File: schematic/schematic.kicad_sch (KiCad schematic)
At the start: 25 parts, among them SW1 SW_SPST, U1 ESP32-S3-DevKitC

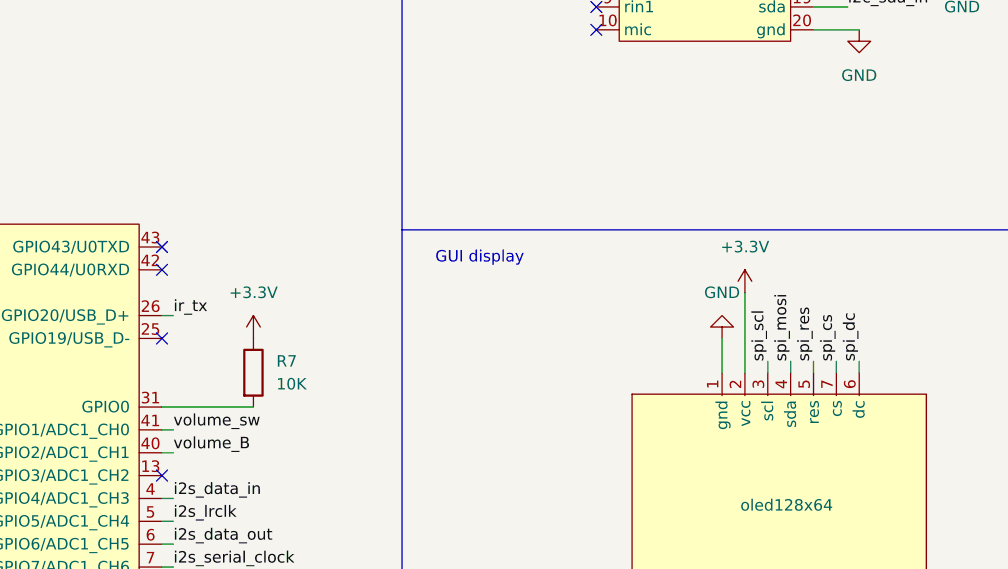
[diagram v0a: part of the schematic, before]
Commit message: Update schematic with note about pullup on GPIO0 for booting from external 5V, bypassing usb.
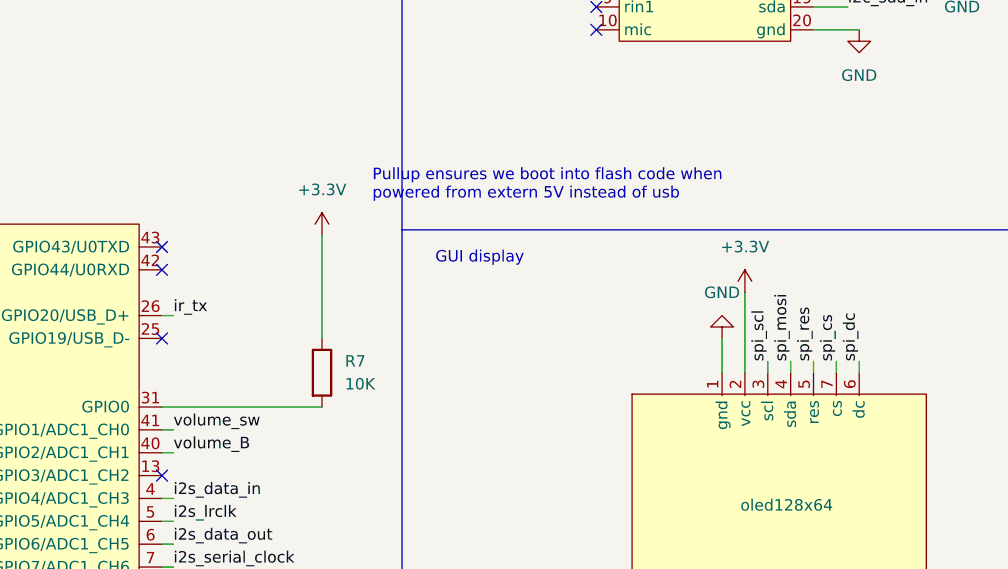
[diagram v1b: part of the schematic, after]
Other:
- note added: "Pullup ensures we boot into flash code when powered from extern 5V instead of usb"
- moved on the sheet: R7
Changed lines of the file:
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@@
 		)
 	)
+	(text "Pullup ensures we boot into flash code when\npowered from extern 5V instead of usb "
+		(exclude_from_sim no)
+		(at 180.848 74.422 0)
+		(effects
+			(font
+				(size 1.27 1.27)
+			)
+			(justify left)
+		)
+	)
 	(text "BOSE IR remote input\nNote: this might not be necessary with\nboot sequence sending AUX and double\nclick on volume sending on/of"
 		(exclude_from_sim no)
@@
 	(wire
 		(pts
+			(xy 175.26 91.44) (xy 175.26 80.01)
+		)
+		(stroke
+			(width 0)
+			(type default)
+		)
+	)
+	(wire
+		(pts
 			(xy 104.14 24.13) (xy 104.14 26.67)
 		)
@@
 	(wire
 		(pts
-			(xy 157.48 99.06) (xy 167.64 99.06)
+			(xy 157.48 99.06) (xy 175.26 99.06)
 		)
 		(stroke
@@
 		)
 		(instances
-			(project ""
+			(project "schematic"
 				(path "/ad99cfc7-1930-4a76-846f-3ad4dbd23fae"
 					(reference "ES8388module")
@@
 		)
 		(instances
-			(project ""
+			(project "schematic"
 				(path "/ad99cfc7-1930-4a76-846f-3ad4dbd23fae"
 					(reference "#PWR04")
@@
 		)
 		(instances
-			(project ""
+			(project "schematic"
 				(path "/ad99cfc7-1930-4a76-846f-3ad4dbd23fae"
 					(reference "#PWR01")
@@
 		)
 		(instances
-			(project ""
+			(project "schematic"
 				(path "/ad99cfc7-1930-4a76-846f-3ad4dbd23fae"
 					(reference "R5")
@@
 		)
 		(instances
-			(project ""
+			(project "schematic"
 				(path "/ad99cfc7-1930-4a76-846f-3ad4dbd23fae"
 					(reference "SW1")
@@
 		)
 		(instances
-			(project ""
+			(project "schematic"
 				(path "/ad99cfc7-1930-4a76-846f-3ad4dbd23fae"
 					(reference "#PWR06")
@@
 		)
 		(instances
-			(project ""
+			(project "schematic"
 				(path "/ad99cfc7-1930-4a76-846f-3ad4dbd23fae"
 					(reference "#PWR027")
@@
 		)
 		(instances
-			(project ""
+			(project "schematic"
 				(path "/ad99cfc7-1930-4a76-846f-3ad4dbd23fae"
 					(reference "#PWR017")
@@
 		)
 		(instances
-			(project ""
+			(project "schematic"
 				(path "/ad99cfc7-1930-4a76-846f-3ad4dbd23fae"
 					(reference "#PWR07")
@@
 		)
 		(instances
-			(project ""
+			(project "schematic"
 				(path "/ad99cfc7-1930-4a76-846f-3ad4dbd23fae"
 					(reference "R10")
@@
 		)
 		(instances
-			(project ""
+			(project "schematic"
 				(path "/ad99cfc7-1930-4a76-846f-3ad4dbd23fae"
 					(reference "C1")
@@
 		)
 		(instances
-			(project ""
+			(project "schematic"
 				(path "/ad99cfc7-1930-4a76-846f-3ad4dbd23fae"
 					(reference "#PWR026")
@@
 		)
 		(instances
-			(project ""
+			(project "schematic"
 				(path "/ad99cfc7-1930-4a76-846f-3ad4dbd23fae"
 					(reference "#PWR05")
@@
 		)
 		(instances
-			(project ""
+			(project "schematic"
 				(path "/ad99cfc7-1930-4a76-846f-3ad4dbd23fae"
 					(reference "#PWR014")
@@
 		)
 		(instances
-			(project ""
+			(project "schematic"
 				(path "/ad99cfc7-1930-4a76-846f-3ad4dbd23fae"
 					(reference "#PWR015")
@@
 		)
 		(instances
-			(project ""
+			(project "schematic"
 				(path "/ad99cfc7-1930-4a76-846f-3ad4dbd23fae"
 					(reference "#PWR03")
@@
 		)
 		(instances
-			(project ""
+			(project "schematic"
 				(path "/ad99cfc7-1930-4a76-846f-3ad4dbd23fae"
 					(reference "#PWR016")
@@
 		)
 		(instances
-			(project ""
+			(project "schematic"
 				(path "/ad99cfc7-1930-4a76-846f-3ad4dbd23fae"
 					(reference "D1")
@@
 		)
 		(instances
-			(project ""
+			(project "schematic"
 				(path "/ad99cfc7-1930-4a76-846f-3ad4dbd23fae"
 					(reference "#PWR09")
@@
 		)
 		(instances
-			(project ""
+			(project "schematic"
 				(path "/ad99cfc7-1930-4a76-846f-3ad4dbd23fae"
 					(reference "#PWR02")
@@
 		)
 		(instances
-			(project ""
+			(project "schematic"
 				(path "/ad99cfc7-1930-4a76-846f-3ad4dbd23fae"
 					(reference "U1")
@@
 		)
 		(instances
-			(project ""
+			(project "schematic"
 				(path "/ad99cfc7-1930-4a76-846f-3ad4dbd23fae"
 					(reference "#PWR013")
@@
 		)
 		(instances
-			(project ""
+			(project "schematic"
 				(path "/ad99cfc7-1930-4a76-846f-3ad4dbd23fae"
 					(reference "oled128x64")
@@
 		)
 		(instances
-			(project ""
+			(project "schematic"
 				(path "/ad99cfc7-1930-4a76-846f-3ad4dbd23fae"
 					(reference "#PWR010")
@@
 		)
 		(instances
-			(project ""
+			(project "schematic"
 				(path "/ad99cfc7-1930-4a76-846f-3ad4dbd23fae"
 					(reference "#PWR028")
@@
 	(symbol
 		(lib_id "Device:R")
-		(at 167.64 95.25 0)
+		(at 175.26 95.25 0)
 		(unit 1)
 		(exclude_from_sim no)
@@
 		(fields_autoplaced yes)
 		(property "Reference" "R7"
-			(at 170.18 93.9799 0)
+			(at 177.8 93.9799 0)
 			(effects
 				(font
@@
 		)
 		(property "Value" "10K"
-			(at 170.18 96.5199 0)
+			(at 177.8 96.5199 0)
 			(effects
 				(font
@@
 		)
 		(property "Footprint" ""
-			(at 165.862 95.25 90)
+			(at 173.482 95.25 90)
 			(effects
 				(font
@@
 		)
 		(property "Datasheet" "~"
-			(at 167.64 95.25 0)
+			(at 175.26 95.25 0)
 			(effects
 				(font
@@
 		)
 		(property "Description" "Resistor"
-			(at 167.64 95.25 0)
+			(at 175.26 95.25 0)
 			(effects
 				(font
@@
 		)
 		(instances
-			(project ""
+			(project "schematic"
 				(path "/ad99cfc7-1930-4a76-846f-3ad4dbd23fae"
 					(reference "R7")
@@
 		)
 		(instances
-			(project ""
+			(project "schematic"
 				(path "/ad99cfc7-1930-4a76-846f-3ad4dbd23fae"
 					(reference "#PWR019")
@@
 	(symbol
 		(lib_id "power:+3.3V")
-		(at 167.64 91.44 0)
+		(at 175.26 80.01 0)
 		(unit 1)
 		(exclude_from_sim no)
@@
 		(fields_autoplaced yes)
 		(property "Reference" "#PWR029"
-			(at 167.64 95.25 0)
+			(at 175.26 83.82 0)
 			(effects
 				(font
@@
 		)
 		(property "Value" "+3.3V"
-			(at 167.64 86.36 0)
+			(at 175.26 74.93 0)
 			(effects
 				(font
@@
 		)
 		(property "Footprint" ""
-			(at 167.64 91.44 0)
+			(at 175.26 80.01 0)
 			(effects
 				(font
@@
 		)
 		(property "Datasheet" ""
-			(at 167.64 91.44 0)
+			(at 175.26 80.01 0)
 			(effects
 				(font
@@
 		)
 		(property "Description" "Power symbol creates a global label with name \"+3.3V\""
-			(at 167.64 91.44 0)
+			(at 175.26 80.01 0)
 			(effects
 				(font
@@
 		)
 		(instances
-			(project ""
+			(project "schematic"
 				(path "/ad99cfc7-1930-4a76-846f-3ad4dbd23fae"
 					(reference "#PWR029")
@@
 		)
 		(instances
-			(project ""
+			(project "schematic"
 				(path "/ad99cfc7-1930-4a76-846f-3ad4dbd23fae"
 					(reference "R2")
@@
 		)
 		(instances
-			(project ""
+			(project "schematic"
 				(path "/ad99cfc7-1930-4a76-846f-3ad4dbd23fae"
 					(reference "volume")
@@
 		)
 		(instances
-			(project ""
+			(project "schematic"
 				(path "/ad99cfc7-1930-4a76-846f-3ad4dbd23fae"
 					(reference "C3")
@@
 		)
 		(instances
-			(project ""
+			(project "schematic"
 				(path "/ad99cfc7-1930-4a76-846f-3ad4dbd23fae"
 					(reference "R1")
@@
 		)
 		(instances
-			(project ""
+			(project "schematic"
 				(path "/ad99cfc7-1930-4a76-846f-3ad4dbd23fae"
 					(reference "bose_on_sw")
@@
 		)
 		(instances
-			(project ""
+			(project "schematic"
 				(path "/ad99cfc7-1930-4a76-846f-3ad4dbd23fae"
 					(reference "#PWR08")

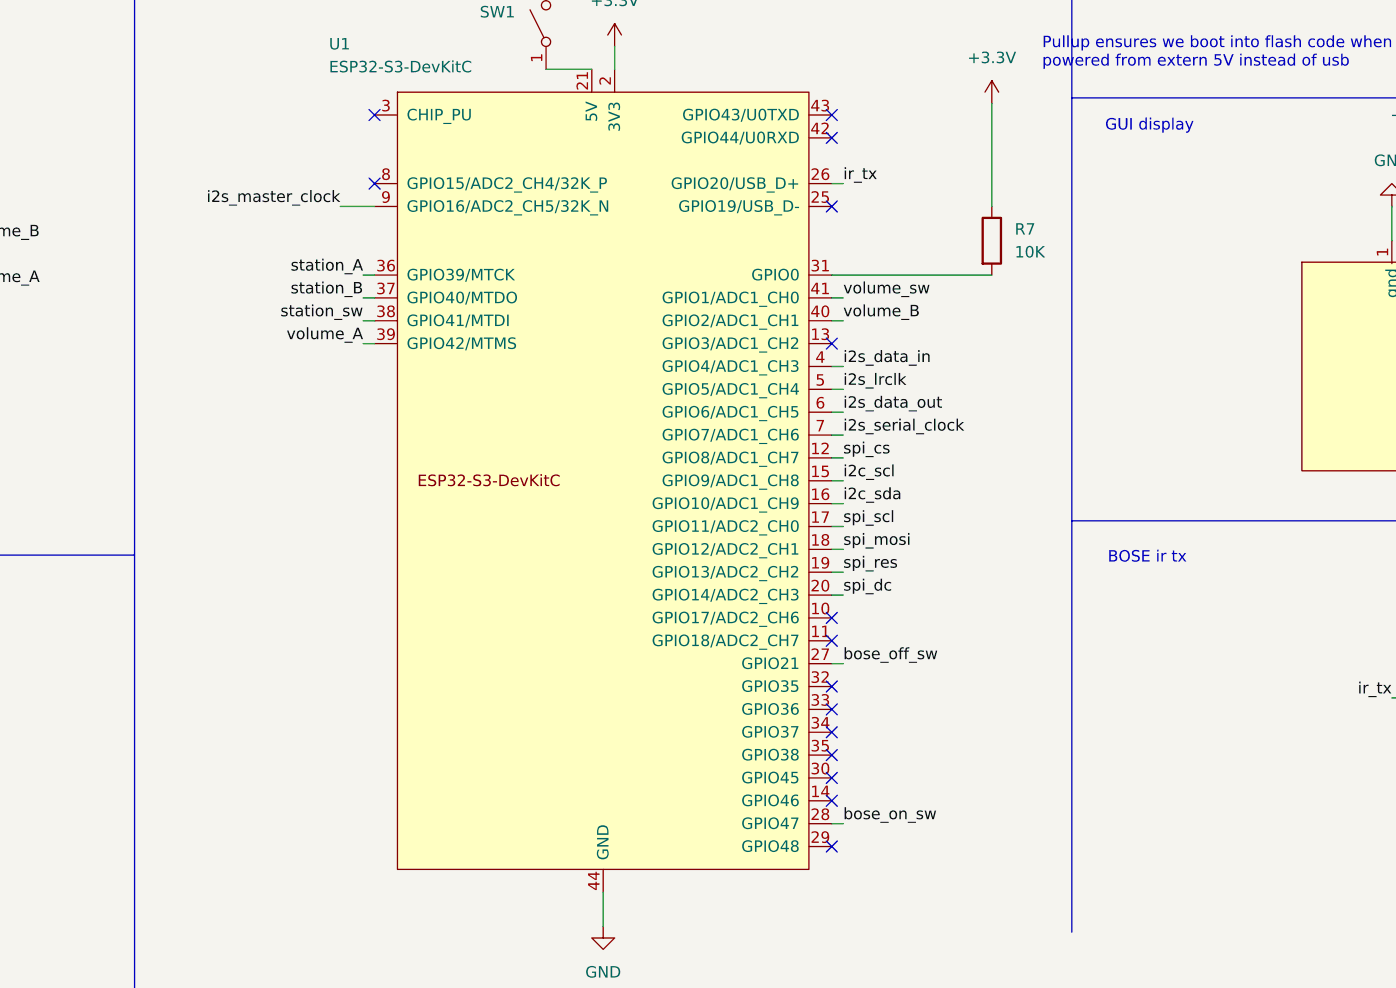
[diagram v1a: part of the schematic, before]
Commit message: update gpio assignments on schematic.
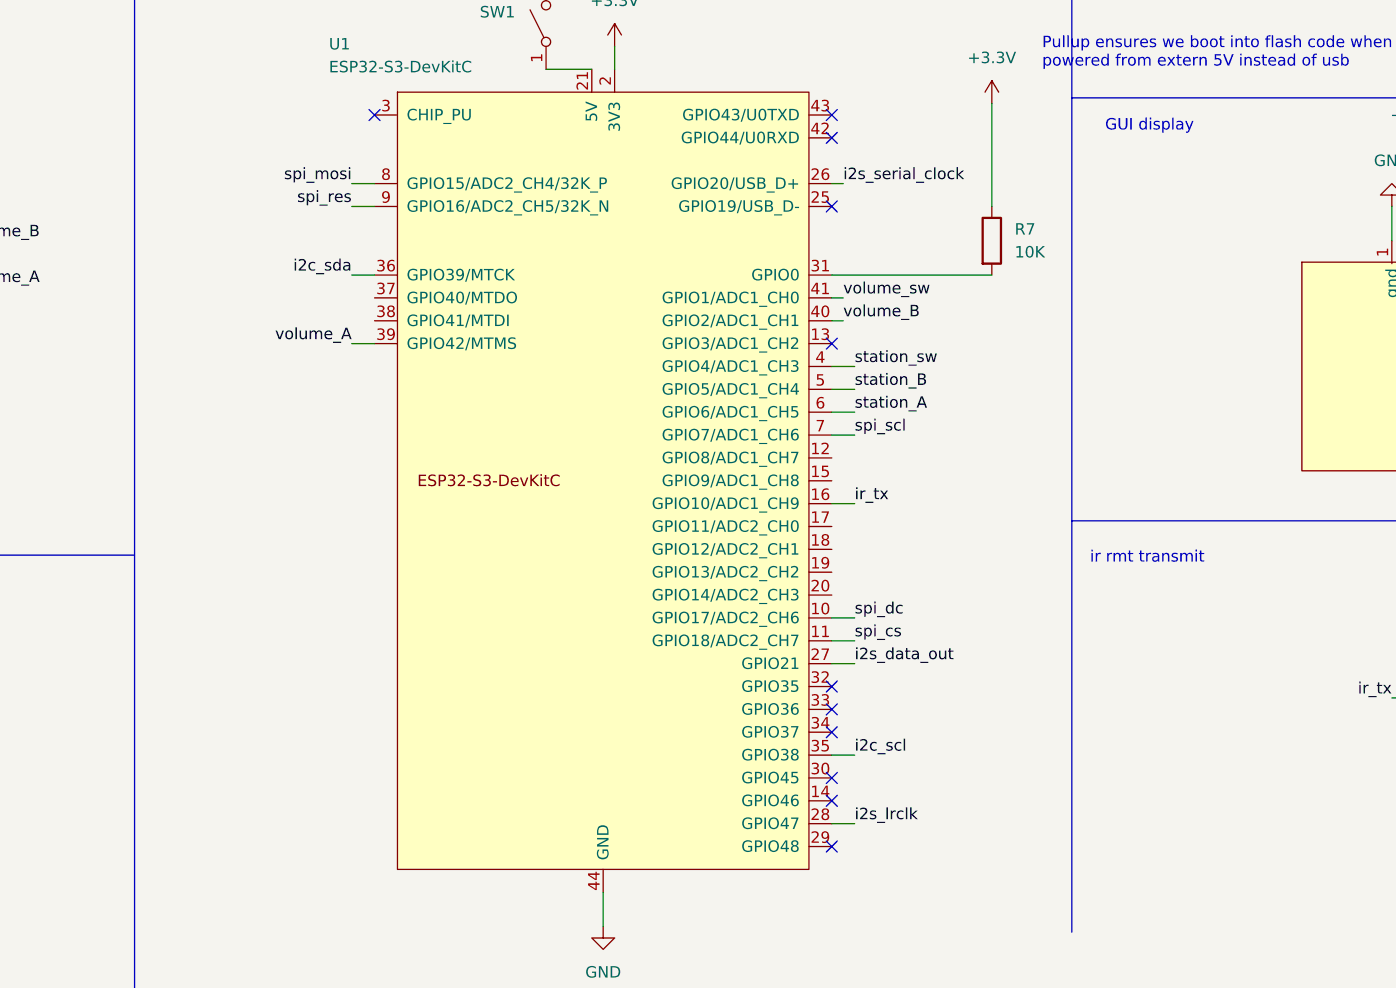
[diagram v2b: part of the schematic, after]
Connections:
- net bose_off_sw: no longer U1.27 (GPIO21)
- net bose_on_sw: no longer U1.28 (GPIO47)
- net i2c_scl: now also U1.35 (GPIO38); no longer U1.15 (GPIO9/ADC1_CH8)
- net i2c_sda: now also U1.36 (GPIO39/MTCK); no longer U1.16 (GPIO10/ADC1_CH9)
- net i2s_data_in: no longer U1.4 (GPIO4/ADC1_CH3)
- net i2s_data_out: now also U1.27 (GPIO21); no longer U1.6 (GPIO6/ADC1_CH5)
- net i2s_lrclk: now also U1.28 (GPIO47); no longer U1.5 (GPIO5/ADC1_CH4)
- net i2s_master_clock: no longer U1.9 (GPIO16/ADC2_CH5/32K_N)
- net i2s_serial_clock: now also U1.26 (GPIO20/USB_D+); no longer U1.7 (GPIO7/ADC1_CH6)
- net ir_tx: now also U1.16 (GPIO10/ADC1_CH9); no longer U1.26 (GPIO20/USB_D+)
- net spi_cs: now also U1.11 (GPIO18/ADC2_CH7); no longer U1.12 (GPIO8/ADC1_CH7)
- net spi_dc: now also U1.10 (GPIO17/ADC2_CH6); no longer U1.20 (GPIO14/ADC2_CH3)
- net spi_mosi: now also U1.8 (GPIO15/ADC2_CH4/32K_P); no longer U1.18 (GPIO12/ADC2_CH1)
- net spi_res: now also U1.9 (GPIO16/ADC2_CH5/32K_N); no longer U1.19 (GPIO13/ADC2_CH2)
- net spi_scl: now also U1.7 (GPIO7/ADC1_CH6); no longer U1.17 (GPIO11/ADC2_CH0)
- net station_A: now also U1.6 (GPIO6/ADC1_CH5); no longer U1.36 (GPIO39/MTCK)
- net station_B: now also U1.5 (GPIO5/ADC1_CH4); no longer U1.37 (GPIO40/MTDO)
- net station_sw: now also U1.4 (GPIO4/ADC1_CH3); no longer U1.38 (GPIO41/MTDI)
- no-connect marks 23 -> 19
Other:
- note added: "ir rmt transmit"
- note removed: "BOSE ir tx"
